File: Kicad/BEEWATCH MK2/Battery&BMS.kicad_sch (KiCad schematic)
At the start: 22 parts, among them Q3 DMP1045U-7, Q9 DMG6968U, U4 MCP73832-2-OT, U5 ME6217C33M5G, U8 S-1206B18-M3T1G

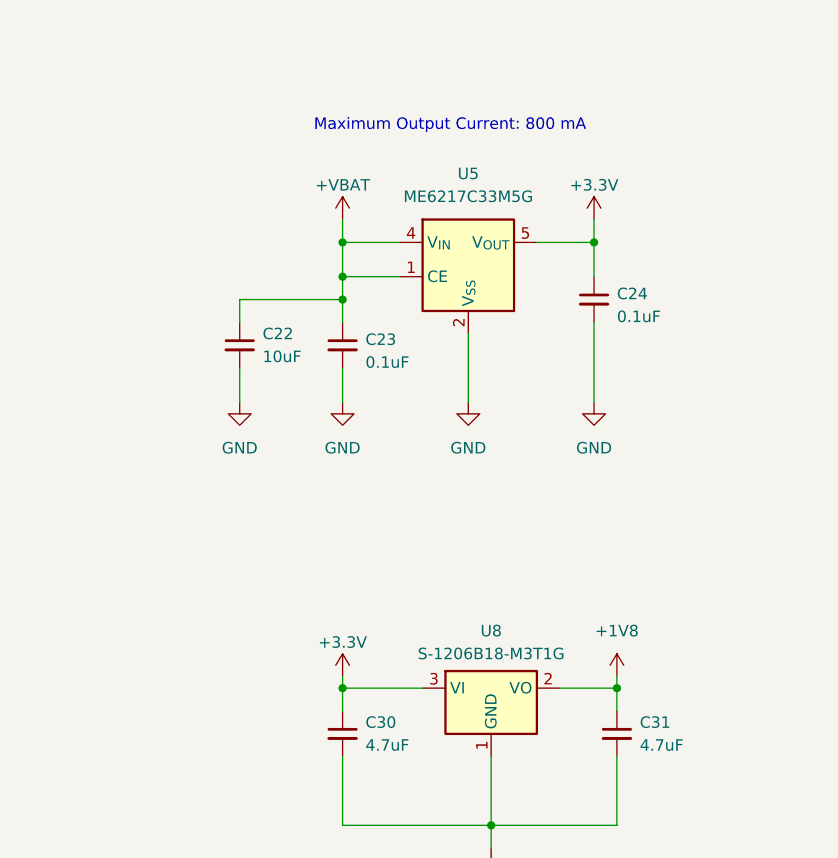
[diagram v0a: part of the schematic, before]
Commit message: Schematic changes
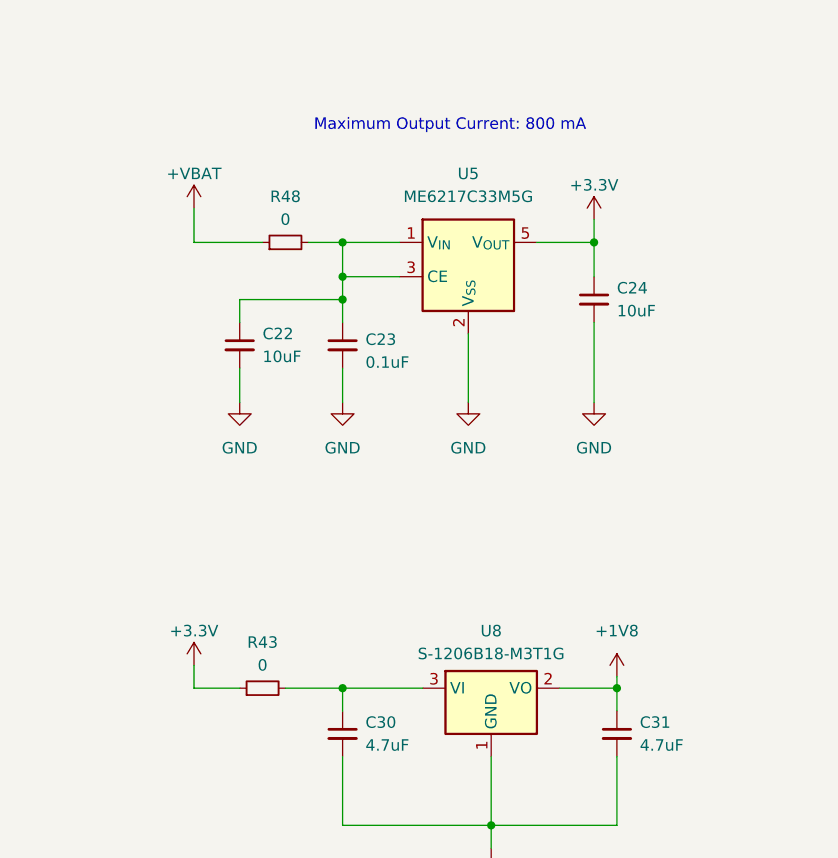
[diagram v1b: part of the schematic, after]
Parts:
- added R43, R48: 0, Resistor_SMD:R_0402_1005Metric_Pad0.72x0.64mm_HandSolder, symbol Device:R_Small
- C22, C23: footprint Capacitor_SMD:C_0603_1608Metric -> Capacitor_SMD:C_0402_1005Metric_Pad0.74x0.62mm_HandSolder
- C24: value 0.1uF -> 10uF
- R20, R21, R22, R44, R45, R46, R47: footprint Resistor_SMD:R_0402_1005Metric -> Resistor_SMD:R_0402_1005Metric_Pad0.72x0.64mm_HandSolder
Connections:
- net +3.3V: now also R43.1; no longer C30.1, U8.3 (VI)
- net +VBAT: now also R48.1; no longer C22.1, C23.1, U5.1 (CE), U5.4 (V_{IN})
- net at U5.3 (CE): now also C22.1, C23.1, U5.1 (V_{IN}), R48.2
- new net: C30.1, R43.2, U8.3 (VI)

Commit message: GNSS level shifter floating voltage needs to be fix
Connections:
- net +VBAT: now also C22.1, C23.1, R48.2, U5.1 (V_{IN}), U5.3 (CE)
- net +3V3: now reaches C30.1, R43.2, U8.3 (VI)
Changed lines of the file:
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@@
+		)
+	)
+	(label "+3V3"
+		(at 209.55 106.68 0)
+		(effects
+			(font
+				(size 1.27 1.27)
+			)
+			(justify left bottom)
 		)
 	)
@@
 		(effects
 			(font
+				(size 1.27 1.27)
+			)
+			(justify left bottom)
+		)
+	)
+	(label "+VBAT"
+		(at 209.55 57.15 0)
+		(effects
+			(font

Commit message: Added Buzzer flyback diode
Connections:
- net +VBAT: no longer C22.1, C23.1, R48.2, U5.1 (V_{IN}), U5.3 (CE)
- net +3V3 renamed +3V3_IN
- new net +VBAT_IN: C22.1, C23.1, R48.2, U5.1 (V_{IN}), U5.3 (CE)
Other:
- moved on the sheet: BT1, C19, C20, C21, D2, Q3, Q9, R20, R21, R22, R44, R45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

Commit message: Updated with sub module lib
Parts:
- BT1: footprint Project:WLY902025 -> BATTERY:WLY902025
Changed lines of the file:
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@@
 			)
 		)
-		(property "Footprint" "Project:WLY902025"
+		(property "Footprint" "BATTERY:WLY902025"
 			(at 107.95 68.326 90)
 			(effects

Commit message: ERC Checking
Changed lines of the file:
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@@
 	(wire
 		(pts
-			(xy 218.44 106.68) (xy 209.55 106.68)
+			(xy 209.55 106.68) (xy 218.44 106.68)
 		)
 		(stroke
@@
 	(wire
 		(pts
+			(xy 209.55 53.34) (xy 209.55 57.15)
+		)
+		(stroke
+			(width 0)
+			(type default)
+		)
+	)
+	(wire
+		(pts
 			(xy 78.74 179.07) (xy 88.9 179.07)
 		)
@@
 	)
 	(label "+3V3_IN"
-		(at 204.47 106.68 0)
+		(at 210.82 106.68 0)
 		(effects
 			(font
@@
 	)
 	(symbol
+		(lib_id "power:PWR_FLAG")
+		(at 209.55 53.34 0)
+		(unit 1)
+		(exclude_from_sim no)
+		(in_bom yes)
+		(on_board yes)
+		(dnp no)
+		(fields_autoplaced yes)
+		(property "Reference" "#FLG03"
+			(at 209.55 51.435 0)
+			(effects
+				(font
+					(size 1.27 1.27)
+				)
+				(hide yes)
+			)
+		)
+		(property "Value" "+VBAT_IN"
+			(at 209.55 48.26 0)
+			(effects
+				(font
+					(size 1.27 1.27)
+				)
+			)
+		)
+		(property "Footprint" ""
+			(at 209.55 53.34 0)
+			(effects
+				(font
+					(size 1.27 1.27)
+				)
+				(hide yes)
+			)
+		)
+		(property "Datasheet" "~"
+			(at 209.55 53.34 0)
+			(effects
+				(font
+					(size 1.27 1.27)
+				)
+				(hide yes)
+			)
+		)
+		(property "Description" "Special symbol for telling ERC where power comes from"
+			(at 209.55 53.34 0)
+			(effects
+				(font
+					(size 1.27 1.27)
+				)
+				(hide yes)
+			)
+		)
+		(pin "1"
+		)
+		(instances
+			(project "BEEWATCH MK2"
+				(path "/e9c5fb53-480b-4989-8495-a3341ee99514/d9595010-f994-473f-a0a5-39e7f06951fe"
+					(reference "#FLG03")
+					(unit 1)
+				)
+			)
+		)
+	)
+	(symbol
 		(lib_id "Device:R_Small")
 		(at 49.53 72.39 0)
@@
 					(unit 1)
 				)
+			)
+		)
+	)
+	(symbol
+		(lib_id "power:PWR_FLAG")
+		(at 209.55 106.68 0)
+		(unit 1)
+		(exclude_from_sim no)
+		(in_bom yes)
+		(on_board yes)
+		(dnp no)
+		(fields_autoplaced yes)
+		(property "Reference" "#FLG02"
+			(at 209.55 104.775 0)
+			(effects
+				(font
+					(size 1.27 1.27)
+				)
+				(hide yes)
+			)
+		)
+		(property "Value" "+3V3_IN"
+			(at 209.55 101.6 0)
+			(effects
+				(font
+					(size 1.27 1.27)
+				)
+			)
+		)
+		(property "Footprint" ""
+			(at 209.55 106.68 0)
+			(effects
+				(font
+					(size 1.27 1.27)
+				)
+				(hide yes)
+			)
+		)
+		(property "Datasheet" "~"
+			(at 209.55 106.68 0)
+			(effects
+				(font
+					(size 1.27 1.27)
+				)
+				(hide yes)
+			)
+		)
+		(property "Description" "Special symbol for telling ERC where power comes from"
+			(at 209.55 106.68 0)
+			(effects
+				(font
+					(size 1.27 1.27)
+				)
+				(hide yes)
+			)
+		)
+		(pin "1"
+		)
+		(instances
+			(project ""
+				(path "/e9c5fb53-480b-4989-8495-a3341ee99514/d9595010-f994-473f-a0a5-39e7f06951fe"
+					(reference "#FLG02")
+					(unit 1)
+				)

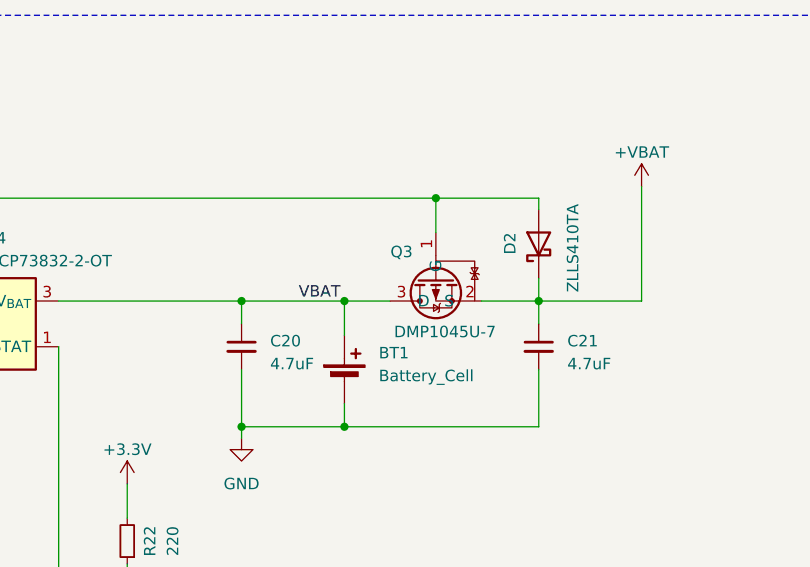
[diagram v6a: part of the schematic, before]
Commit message: ERC going on anf All Lib issue is fixed
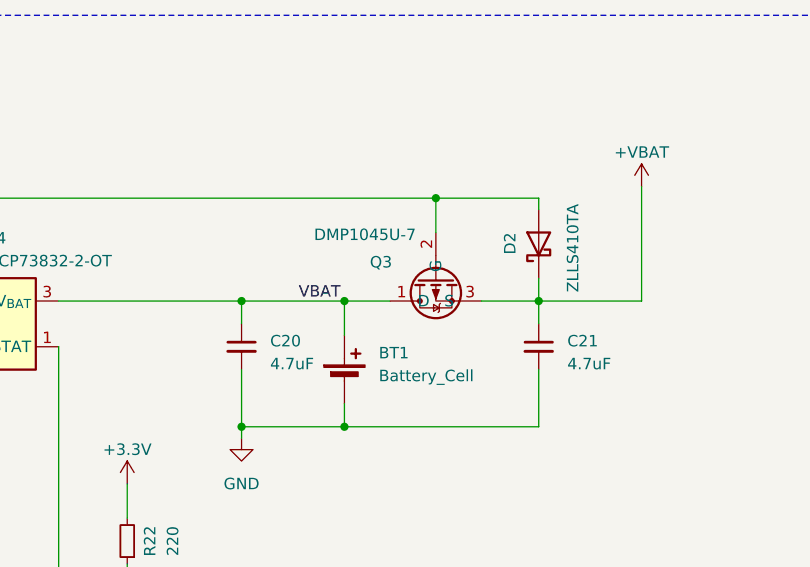
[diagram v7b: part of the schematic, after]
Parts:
- removed Q3: DMP1045U-7, Package_TO_SOT_SMD:SOT-23-3, symbol Project_Library:DMP1045U-7
- added Q3: DMP1045U-7, Package_TO_SOT_SMD:SOT-23-3, symbol SM_PMOS:DMP1045U-7
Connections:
- net +VBAT: now also Q3.3 (S)
- net VBAT: now also Q3.1 (D)
- net VBUS: now also Q3.2 (G)
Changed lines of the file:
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@@
+	)
+	(symbol
+		(lib_id "SM_PMOS:DMP1045U-7")
+		(at 118.11 60.96 90)
+		(mirror x)
+		(unit 1)
+		(exclude_from_sim no)
+		(in_bom yes)
+		(on_board yes)
+		(dnp no)
+		(property "Reference" "Q3"
+			(at 112.014 56.642 90)
+			(effects
+				(font
+					(size 1.27 1.27)
+				)
+			)
+		)
+		(property "Value" "DMP1045U-7"
+			(at 110.236 53.594 90)
+			(effects
+				(font
+					(size 1.27 1.27)
+				)
+			)
+		)
+		(property "Footprint" "Package_TO_SOT_SMD:SOT-23-3"
+			(at 118.11 60.96 0)
+			(effects
+				(font
+					(size 1.27 1.27)
+				)
+				(hide yes)
+			)
+		)
+		(property "Datasheet" ""
+			(at 118.11 60.96 0)
+			(effects
+				(font
+					(size 1.27 1.27)
+				)
+				(hide yes)
+			)
+		)
+		(property "Description" ""
+			(at 118.11 60.96 0)
+			(effects
+				(font
+					(size 1.27 1.27)
+				)
+				(hide yes)
+			)
+		)
+		(pin "3"
+		)
+		(pin "1"
+		)
+		(pin "2"
+		)
+		(instances
+			(project ""
+				(path "/e9c5fb53-480b-4989-8495-a3341ee99514/d9595010-f994-473f-a0a5-39e7f06951fe"
+					(reference "Q3")
+					(unit 1)
+				)
+			)
+		)
 	)
 	(symbol
@@
 					(unit 1)
 				)
-			)
-		)
-	)
-	(symbol
-		(lib_id "Project_Library:DMP1045U-7")
-		(at 118.11 57.15 90)
-		(mirror x)
-		(unit 1)
-		(exclude_from_sim no)
-		(in_bom yes)
-		(on_board yes)
-		(dnp no)
-		(property "Reference" "Q3"
-			(at 114.3 55.499 90)
-			(effects
-				(font
-					(size 1.27 1.27)
-				)
-			)
-		)
-		(property "Value" "DMP1045U-7"
-			(at 119.126 64.389 90)
-			(effects
-				(font
-					(size 1.27 1.27)
-				)
-			)
-		)
-		(property "Footprint" "Package_TO_SOT_SMD:SOT-23-3"
-			(at 101.6 59.69 0)
-			(effects
-				(font
-					(size 1.27 1.27)
-				)
-				(hide yes)
-			)
-		)
-		(property "Datasheet" ""
-			(at 114.3 55.88 0)
-			(effects
-				(font
-					(size 1.27 1.27)
-				)
-				(hide yes)
-			)
-		)
-		(property "Description" ""
-			(at 118.11 57.15 0)
-			(effects
-				(font
-					(size 1.27 1.27)
-				)
-				(hide yes)
-			)
-		)
-		(pin "1"
-		)
-		(pin "2"
-		)
-		(pin "3"
-		)
-		(instances
-			(project "BEEWATCH"
-				(path "/e9c5fb53-480b-4989-8495-a3341ee99514/d9595010-f994-473f-a0a5-39e7f06951fe"
-					(reference "Q3")
-					(unit 1)
-				)

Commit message: ERC Checking
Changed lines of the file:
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@@
 	)
 	(junction
-		(at 226.06 121.92)
-		(diameter 0)
-		(color 0 0 0 0)
-	)
-	(junction
 		(at 237.49 57.15)
 		(diameter 0)
@@
 	(wire
 		(pts
-			(xy 240.03 114.3) (xy 240.03 121.92)
+			(xy 240.03 114.3) (xy 240.03 125.73)
 		)
 		(stroke
@@
 	(wire
 		(pts
-			(xy 226.06 121.92) (xy 209.55 121.92)
-		)
-		(stroke
-			(width 0)
-			(type default)
-		)
-	)
-	(wire
-		(pts
 			(xy 193.04 57.15) (xy 200.66 57.15)
 		)
@@
 	(wire
 		(pts
-			(xy 209.55 121.92) (xy 209.55 114.3)
+			(xy 209.55 114.3) (xy 209.55 125.73)
 		)
 		(stroke
@@
 	(wire
 		(pts
-			(xy 193.04 106.68) (xy 198.12 106.68)
+			(xy 226.06 114.3) (xy 226.06 125.73)
 		)
 		(stroke
@@
 	(wire
 		(pts
-			(xy 233.68 106.68) (xy 240.03 106.68)
+			(xy 193.04 106.68) (xy 198.12 106.68)
 		)
 		(stroke
@@
 	(wire
 		(pts
-			(xy 209.55 71.12) (xy 209.55 74.93)
+			(xy 233.68 106.68) (xy 240.03 106.68)
 		)
 		(stroke
@@
 	(wire
 		(pts
-			(xy 226.06 121.92) (xy 226.06 124.46)
+			(xy 209.55 71.12) (xy 209.55 74.93)
 		)
 		(stroke
@@
 	(wire
 		(pts
-			(xy 209.55 53.34) (xy 209.55 57.15)
-		)
-		(stroke
-			(width 0)
-			(type default)
-		)
-	)
-	(wire
-		(pts
 			(xy 78.74 179.07) (xy 88.9 179.07)
 		)
@@
 	(wire
 		(pts
-			(xy 226.06 114.3) (xy 226.06 121.92)
-		)
-		(stroke
-			(width 0)
-			(type default)
-		)
-	)
-	(wire
-		(pts
 			(xy 205.74 57.15) (xy 209.55 57.15)
 		)
@@
 	(wire
 		(pts
-			(xy 240.03 121.92) (xy 226.06 121.92)
-		)
-		(stroke
-			(width 0)
-			(type default)
-		)
-	)
-	(wire
-		(pts
 			(xy 209.55 57.15) (xy 209.55 60.96)
 		)
@@
 	)
 	(label "+3V3_IN"
-		(at 210.82 106.68 0)
+		(at 207.01 106.68 0)
 		(effects
 			(font
@@
 	(symbol
 		(lib_id "power:GND")
+		(at 209.55 125.73 0)
+		(unit 1)
+		(exclude_from_sim no)
+		(in_bom yes)
+		(on_board yes)
+		(dnp no)
+		(fields_autoplaced yes)
+		(property "Reference" "#PWR080"
+			(at 209.55 132.08 0)
+			(effects
+				(font
+					(size 1.27 1.27)
+				)
+				(hide yes)
+			)
+		)
+		(property "Value" "GND"
+			(at 209.55 130.81 0)
+			(effects
+				(font
+					(size 1.27 1.27)
+				)
+			)
+		)
+		(property "Footprint" ""
+			(at 209.55 125.73 0)
+			(effects
+				(font
+					(size 1.27 1.27)
+				)
+				(hide yes)
+			)
+		)
+		(property "Datasheet" ""
+			(at 209.55 125.73 0)
+			(effects
+				(font
+					(size 1.27 1.27)
+				)
+				(hide yes)
+			)
+		)
+		(property "Description" "Power symbol creates a global label with name \"GND\" , ground"
+			(at 209.55 125.73 0)
+			(effects
+				(font
+					(size 1.27 1.27)
+				)
+				(hide yes)
+			)
+		)
+		(pin "1"
+		)
+		(instances
+			(project "BEEWATCH MK2"
+				(path "/e9c5fb53-480b-4989-8495-a3341ee99514/d9595010-f994-473f-a0a5-39e7f06951fe"
+					(reference "#PWR080")
+					(unit 1)
+				)
+			)
+		)
+	)
+	(symbol
+		(lib_id "power:GND")
 		(at 237.49 74.93 0)
 		(unit 1)
@@
 	(symbol
 		(lib_id "power:GND")
-		(at 226.06 124.46 0)
+		(at 226.06 125.73 0)
 		(unit 1)
 		(exclude_from_sim no)
@@
 		(fields_autoplaced yes)
 		(property "Reference" "#PWR076"
-			(at 226.06 130.81 0)
+			(at 226.06 132.08 0)
 			(effects
 				(font
@@
 		)
 		(property "Value" "GND"
-			(at 226.06 129.54 0)
+			(at 226.06 130.81 0)
 			(effects
 				(font
@@
 		)
 		(property "Footprint" ""
-			(at 226.06 124.46 0)
+			(at 226.06 125.73 0)
 			(effects
 				(font
@@
 		)
 		(property "Datasheet" ""
-			(at 226.06 124.46 0)
+			(at 226.06 125.73 0)
 			(effects
 				(font
@@
 		)
 		(property "Description" "Power symbol creates a global label with name \"GND\" , ground"
-			(at 226.06 124.46 0)
+			(at 226.06 125.73 0)
 			(effects
 				(font
@@
 	)
 	(symbol
-		(lib_id "power:PWR_FLAG")
-		(at 209.55 53.34 0)
-		(unit 1)
-		(exclude_from_sim no)
-		(in_bom yes)
-		(on_board yes)
-		(dnp no)
-		(fields_autoplaced yes)
-		(property "Reference" "#FLG03"
-			(at 209.55 51.435 0)
-			(effects
-				(font
-					(size 1.27 1.27)
-				)
-				(hide yes)
-			)
-		)
-		(property "Value" "+VBAT_IN"
-			(at 209.55 48.26 0)
-			(effects
-				(font
-					(size 1.27 1.27)
-				)
-			)
-		)
-		(property "Footprint" ""
-			(at 209.55 53.34 0)
-			(effects
-				(font
-					(size 1.27 1.27)
-				)
-				(hide yes)
-			)
-		)
-		(property "Datasheet" "~"
-			(at 209.55 53.34 0)
-			(effects
-				(font
-					(size 1.27 1.27)
-				)
-				(hide yes)
-			)
-		)
-		(property "Description" "Special symbol for telling ERC where power comes from"
-			(at 209.55 53.34 0)
-			(effects
-				(font
-					(size 1.27 1.27)
-				)
-				(hide yes)
-			)
-		)
-		(pin "1"
-		)
-		(instances
-			(project "BEEWATCH MK2"
-				(path "/e9c5fb53-480b-4989-8495-a3341ee99514/d9595010-f994-473f-a0a5-39e7f06951fe"
-					(reference "#FLG03")
-					(unit 1)
-				)
-			)
-		)
-	)
-	(symbol
 		(lib_id "Device:R_Small")
 		(at 49.53 72.39 0)
@@
 	)
 	(symbol
-		(lib_id "power:PWR_FLAG")
-		(at 209.55 106.68 0)
+		(lib_id "power:GND")
+		(at 240.03 125.73 0)
 		(unit 1)
 		(exclude_from_sim no)
@@
 		(dnp no)
 		(fields_autoplaced yes)
-		(property "Reference" "#FLG02"
-			(at 209.55 104.775 0)
+		(property "Reference" "#PWR081"
+			(at 240.03 132.08 0)
 			(effects
 				(font
@@
 			)
 		)
-		(property "Value" "+3V3_IN"
-			(at 209.55 101.6 0)
+		(property "Value" "GND"
+			(at 240.03 130.81 0)
 			(effects
 				(font
@@
 		)
 		(property "Footprint" ""
-			(at 209.55 106.68 0)
+			(at 240.03 125.73 0)
 			(effects
 				(font
@@
 			)
 		)
-		(property "Datasheet" "~"
-			(at 209.55 106.68 0)
+		(property "Datasheet" ""
+			(at 240.03 125.73 0)
 			(effects
 				(font
@@
 			)
 		)
-		(property "Description" "Special symbol for telling ERC where power comes from"
-			(at 209.55 106.68 0)
+		(property "Description" "Power symbol creates a global label with name \"GND\" , ground"
+			(at 240.03 125.73 0)
 			(effects
 				(font
@@
 		)
 		(instances
-			(project ""
+			(project "BEEWATCH MK2"
 				(path "/e9c5fb53-480b-4989-8495-a3341ee99514/d9595010-f994-473f-a0a5-39e7f06951fe"
-					(reference "#FLG02")
+					(reference "#PWR081")
 					(unit 1)
 				)
